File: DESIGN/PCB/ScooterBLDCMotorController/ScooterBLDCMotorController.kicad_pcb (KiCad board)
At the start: 2 copper layers, 210.3 x 103.4 mm, 30 parts, among them J1 M1 OUTPUT, J10 RC_ENABLE, J2 M1 INPUT, J3 M2 INPUT, J4 M2 OUTPUT, J5 I2C, J6 TEST SWITCH, J7 RC CH 1, J8 RC CH 2, J9 RC_PWR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

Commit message: Latest PCB and Rev1.0 release
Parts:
- added J11: TO M2 ENCODER, Connector_JST:JST_XH_B5B-XH-A_1x05_P2.50mm_Vertical, F.Cu at (186.4, 107.1)
- added J12: M2 INPUT, Connector_JST:JST_XH_B5B-XH-A_1x05_P2.50mm_Vertical, F.Cu at (162.1, 136.5)
- added REF**: MountingHole_4.5mm, MountingHole:MountingHole_4.5mm, F.Cu at (247.1, 140.2)
- added REF**: MountingHole_3.2mm_M3, MountingHole:MountingHole_3.2mm_M3, F.Cu at (246.9, 119.0)
- added REF**: MountingHole_3.2mm_M3, MountingHole:MountingHole_3.2mm_M3, F.Cu at (50.0, 62.5)
- added REF**: MountingHole_4.5mm, MountingHole:MountingHole_4.5mm, F.Cu at (247.9, 43.7)
- added REF**: MountingHole_3.2mm_M3, MountingHole:MountingHole_3.2mm_M3, F.Cu at (208.4, 62.7)
- added REF**: MountingHole_3.2mm_M3, MountingHole:MountingHole_3.2mm_M3, F.Cu at (88.4, 118.8)
- added REF**: MountingHole_3.2mm_M3, MountingHole:MountingHole_3.2mm_M3, F.Cu at (197.3, 124.6)
- added REF**: MountingHole_4.5mm, MountingHole:MountingHole_4.5mm, F.Cu at (50.8, 43.7)
- added REF**: MountingHole_3.2mm_M3, MountingHole:MountingHole_3.2mm_M3, F.Cu at (100.3, 68.6)
- added REF**: MountingHole_3.2mm_M3, MountingHole:MountingHole_3.2mm_M3, F.Cu at (197.3, 68.6)
- added REF**: MountingHole_4.5mm, MountingHole:MountingHole_4.5mm, F.Cu at (50.0, 140.2)
- added REF**: MountingHole_3.2mm_M3, MountingHole:MountingHole_3.2mm_M3, F.Cu at (100.3, 124.6)
- J2: value M1 INPUT -> TO M1 ENCODER; footprint Connector_JST:JST_XH_B3B-XH-A_1x03_P2.50mm_Vertical -> Connector_JST:JST_XH_B5B-XH-A_1x05_P2.50mm_Vertical
- J3: value M2 INPUT -> M1 INPUT; footprint Connector_JST:JST_XH_B3B-XH-A_1x03_P2.50mm_Vertical -> Connector_JST:JST_XH_B5B-XH-A_1x05_P2.50mm_Vertical
- R1: footprint Resistor_THT:R_Axial_DIN0204_L3.6mm_D1.6mm_P5.08mm_Vertical -> Resistor_THT:R_Axial_DIN0204_L3.6mm_D1.6mm_P7.62mm_Horizontal
- moved J2 46.1 mm to (112.0, 97.0), turned to -90 degrees
- moved J3 29.3 mm to (133.3, 136.3)
- moved J1 9.76 mm to (115.9, 136.3)
- moved C1 5.76 mm to (139.2, 129.7)
- moved C2 5.76 mm to (139.2, 133.7)
- moved C3 5.76 mm to (139.2, 137.8)
- moved J5 5.63 mm to (157.6, 47.8)
- moved J6 5.63 mm to (111.8, 68.4)
- moved J7 5.63 mm to (134.7, 52.9)
- moved U10 5.63 mm to (127.5, 66.7)
- moved U2 5.63 mm to (141.0, 116.7)
- moved U3 5.63 mm to (150.2, 107.8)
- moved U5 5.63 mm to (165.4, 116.7)
- moved U7 5.63 mm to (167.2, 78.6)
- moved U8 5.63 mm to (167.2, 88.3)
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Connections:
- J2 pad 1: /M1 Y -> Net-(J2-Pad1)
- J2 pad 2: /M1 B -> /M1 Y
- J2 pad 3: /M1 G -> /M1 B
- J3 pad 1: /M2 Y -> Net-(J2-Pad1)
- J3 pad 2: /M2 B -> /M1 Y
- J3 pad 3: /M2 G -> /M1 B
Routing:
- net Net-(J11-Pad5): track 0.00 -> 80.2 mm
- net /M2 G: track 31.5 -> 100.9 mm
- net /M2 B: track 27.3 -> 75.7 mm
- net Net-(J2-Pad1): track 0.00 -> 48.1 mm
- net /M1 Y: track 25.8 -> 70.7 mm
- net /M2 Y: track 24.6 -> 69.1 mm
- net Net-(J11-Pad1): track 0.00 -> 39.5 mm
- net /M1 B: track 29.6 -> 68.7 mm
- net /M1 G: track 30.3 -> 65.6 mm
- net Net-(J2-Pad5): track 0.00 -> 33.9 mm
- net Net-(J6-Pad1): track 53.9 -> 57.5 mm
- net /3v: track 168.1 -> 170.1 mm, vias 1 -> 0
- net /M2 SPEED: track 27.8 -> 29.7 mm
- net /M2 BRAKE: track 27.8 -> 29.7 mm
- net /M2 DIR: track 33.4 -> 35.3 mm
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- added copper zone on B.Cu, net /GND
- added copper zone on F.Cu, net /GND
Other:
- board size 210.3 x 103.4 mm -> 210.3 x 109 mm
- board text added: "BLDC MOTOR CONTROLLER REV 1.0"
- board text added: "M1 CONTROLLER"
- board text added: "M2 CONTROLLER"
- board text added: "TO M1 ENCODERS"
- board text added: "TO M2 ENCODERS"

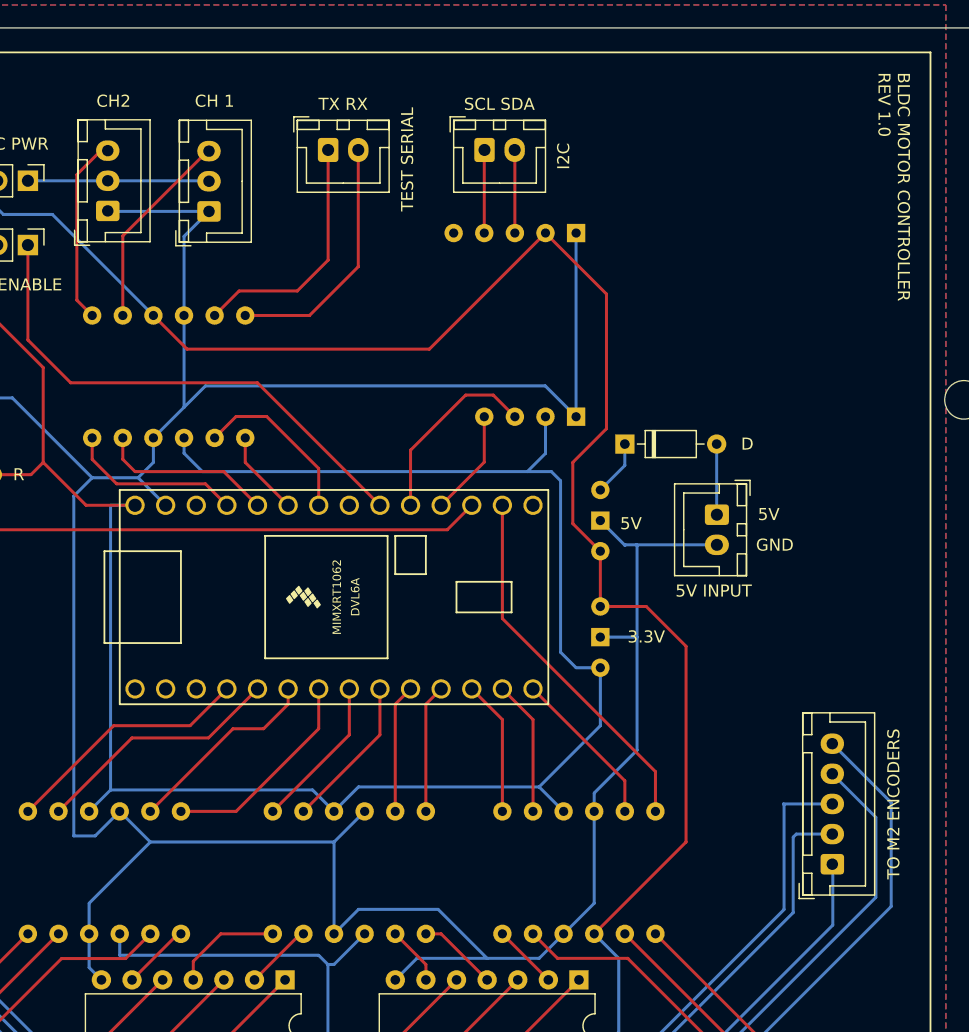
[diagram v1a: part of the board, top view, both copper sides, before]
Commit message: Fixed swapped connections on level shifter.
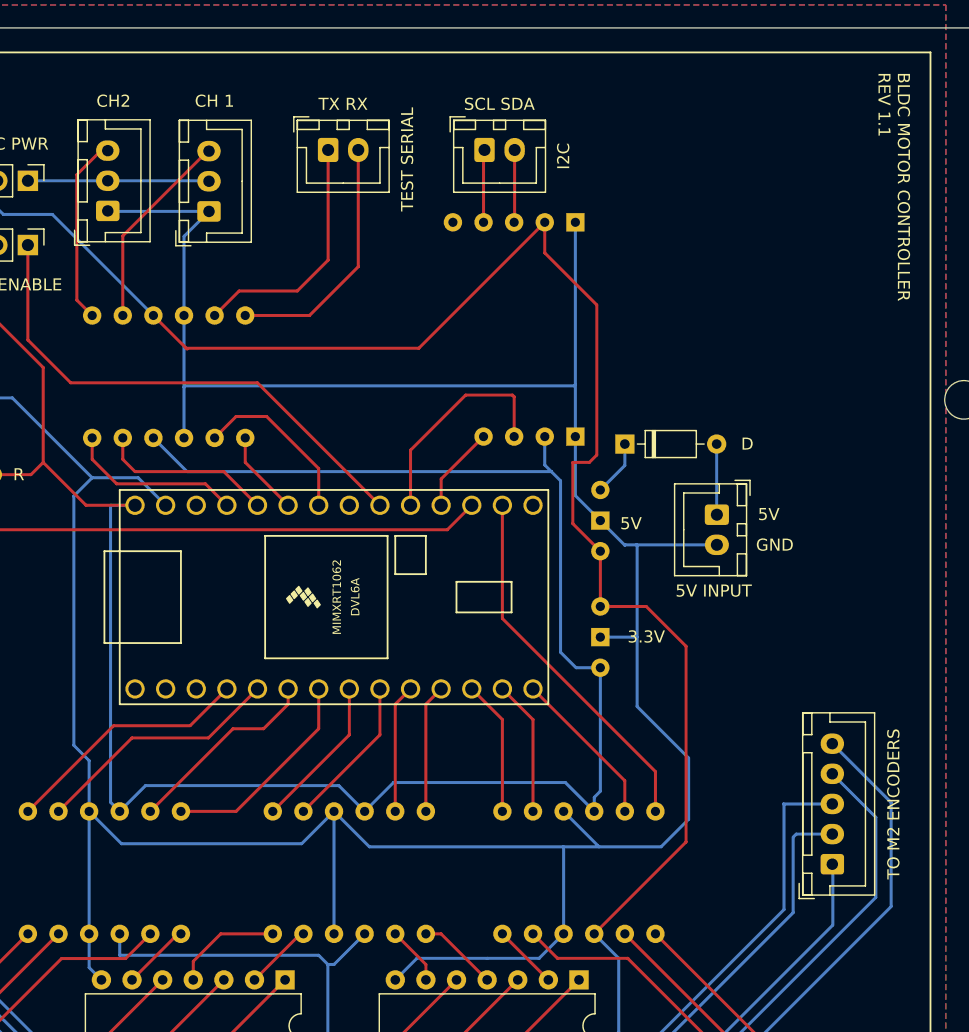
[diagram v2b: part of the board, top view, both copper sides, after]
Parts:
- moved U9 1.65 mm to (162.6, 64.0)
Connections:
- U1 pad 10: /3v -> /GND
- U1 pad 9: /GND -> /3v
- U10 pad 10: /3v -> /GND
- U10 pad 9: /GND -> /3v
- U3 pad 10: /3v -> /GND
- U3 pad 9: /GND -> /3v
- U6 pad 10: /3v -> /GND
- U6 pad 9: /GND -> /3v
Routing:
- net /GND: track 261.1 -> 279.3 mm
- net /3v: track 170.1 -> 172.7 mm
- net Net-(U4-Pad24): track 15.9 -> 18.4 mm
- net Net-(U4-Pad23): track 8.83 -> 7.15 mm
- net /5v: track 233.4 -> 234.8 mm
- net Net-(J5-Pad2): track 6.87 -> 6.02 mm
- net Net-(J5-Pad1): track 6.87 -> 6.04 mm
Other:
- board text added: "BLDC MOTOR CONTROLLER REV 1.1"
- board text removed: "BLDC MOTOR CONTROLLER REV 1.0"

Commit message: Revision 1.2 of MotorController board
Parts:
- added J13: Conn_01x01_Male, Connector_PinHeader_2.54mm:PinHeader_1x01_P2.54mm_Vertical, F.Cu at (111.5, 135.4)
- added J14: Conn_01x01_Male, Connector_PinHeader_2.54mm:PinHeader_1x01_P2.54mm_Vertical, F.Cu at (186.7, 82.8)
- U7: value 5V_Voltage_Regulator -> (none); footprint Custom:Voltage Regulator -> Custom:Level Shifter
- U8: value 3.3V_Voltage_Regulator -> 5V_StepUpDown_Voltage_Regulator; footprint Custom:Voltage Regulator -> Custom:StepUpDown Voltage Regulator
- U9: value (none) -> 3V_StepUpDown_Voltage_Regulator; footprint Custom:I2C Level Shifter -> Custom:StepUpDown Voltage Regulator
- moved J4 93.4 mm to (201.9, 44.5), turned to -90 degrees
- moved J1 89.3 mm to (95.8, 49.3), turned to 90 degrees
- moved U8 31.9 mm to (167.9, 56.4)
- moved D1 25.0 mm to (174.0, 47.8)
- moved POWER1 24.7 mm to (181.6, 53.8)
- moved U7 19.7 mm to (151.4, 66.8)
- moved U9 6.86 mm to (167.9, 68.3), turned to -90 degrees
- moved U4 5.29 mm to (150.4, 84.9)
- moved U1 4.53 mm to (130.8, 103.4)
- moved U3 4.53 mm to (151.1, 103.4)
- moved U6 4.53 mm to (170.2, 103.4)
- moved J6 0.21 mm to (112.0, 68.4)
- moved R1 0.21 mm to (117.0, 74.8)
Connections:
- U7 pad 1: Net-(D1-Pad1) -> unconnected-(U7-Pad1)
- U7 pad 2: /GND -> unconnected-(U7-Pad2)
- U7 pad 3: /5v -> /GND
- U8 pad 1: /5v -> Net-(D1-Pad1)
- U8 pad 3: /3v -> /5v
- U9 pad 2: Net-(U4-Pad23) -> /GND
- U9 pad 3: Net-(U4-Pad24) -> /3v
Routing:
- net /GND: track 279.3 -> 53.6 mm
- net /M1 SPEED: track 32.3 -> 93.3 mm
- net /M1 BRAKE: track 27.1 -> 87.5 mm
- net /M1 DIR: track 27.0 -> 85.7 mm
- net /M2 SPEED: track 29.7 -> 81.4 mm
- net /M2 DIR: track 35.3 -> 86.8 mm
- net /M2 BRAKE: track 29.7 -> 75.5 mm
- net /3v: track 172.7 -> 152.4 mm
- net /5v: track 234.8 -> 247.5 mm
- net Net-(J5-Pad2): track 6.02 -> 17.5 mm
- net Net-(J5-Pad1): track 6.04 -> 17.5 mm
- net Net-(U4-Pad24): track 18.4 -> 10.1 mm
- net Net-(U4-Pad21): track 30.7 -> 24.4 mm
- net Net-(U4-Pad14): track 13.3 -> 7.10 mm
- net Net-(J10-Pad1): track 42.8 -> 48.1 mm
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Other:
- board text added: "BLDC MOTOR CONTROLLER REV 1.2"
- board text removed: "BLDC MOTOR CONTROLLER REV 1.1"

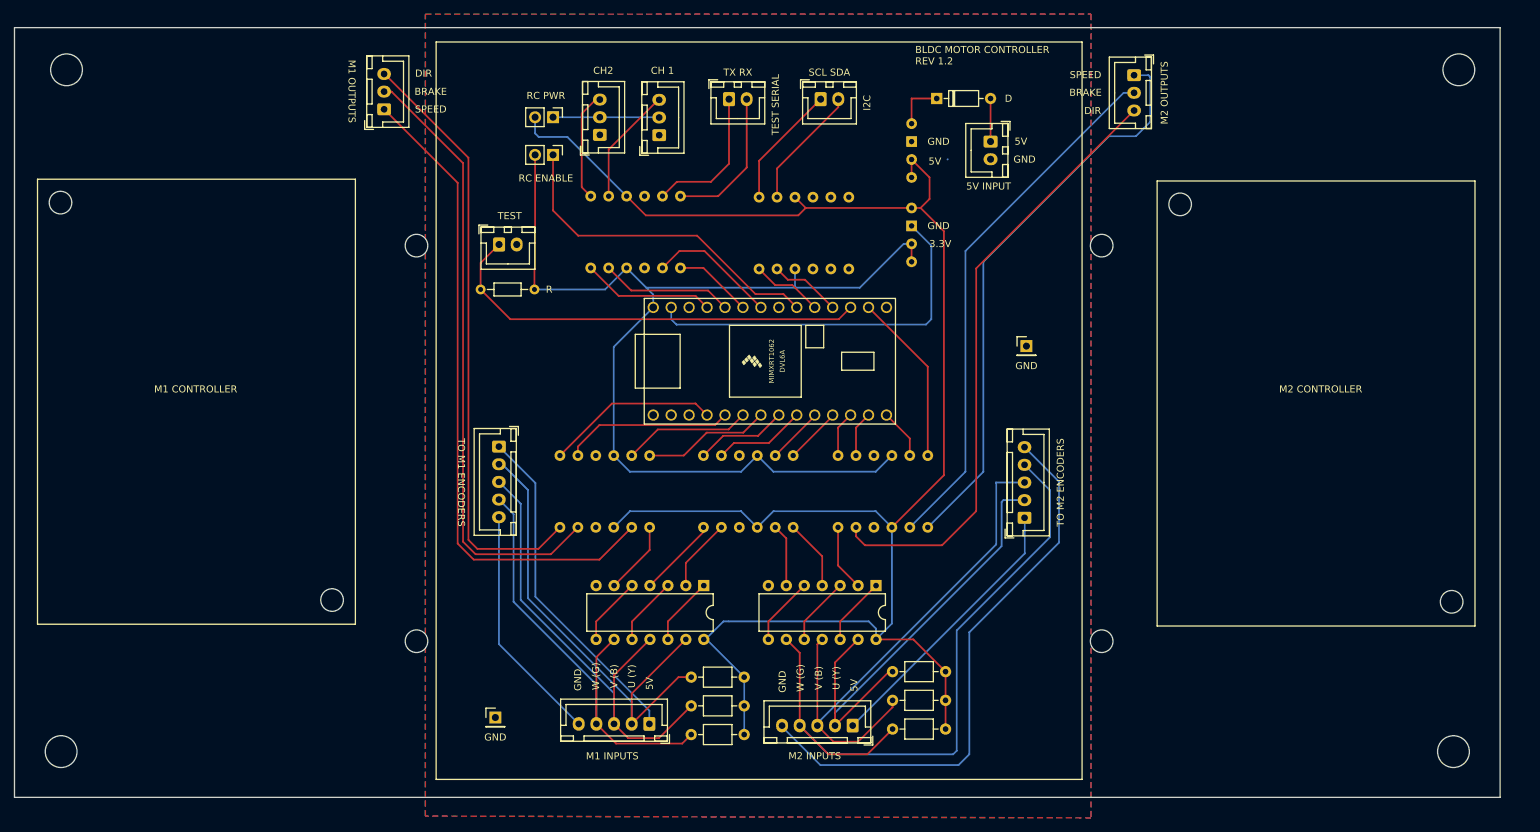
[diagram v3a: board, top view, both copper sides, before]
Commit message: Updated PCB to use terminals, added new DriveByRC code
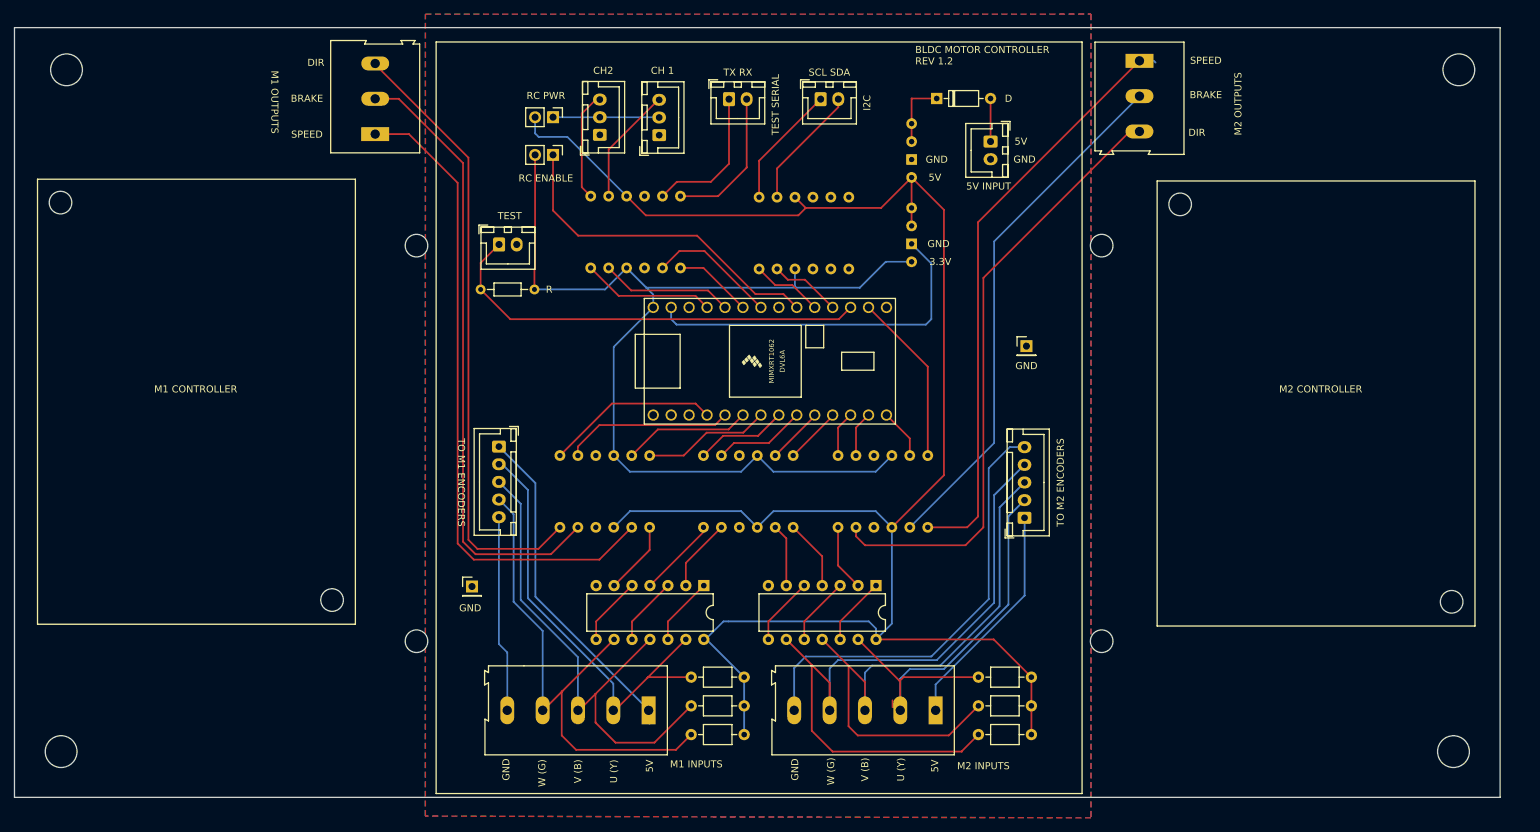
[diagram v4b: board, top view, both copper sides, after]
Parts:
- J1, J4: footprint Connector_JST:JST_XH_B3B-XH-A_1x03_P2.50mm_Vertical -> TerminalBlock:TerminalBlock_Altech_AK300-3_P5.00mm
- J12, J3: footprint Connector_JST:JST_XH_B5B-XH-A_1x05_P2.50mm_Vertical -> Custom:TerminalBlock_Altech_AK300-5_P5.00mm
- moved J13 18.8 mm to (108.2, 116.8)
- moved C4 12.2 mm to (179.9, 129.7)
- moved C5 12.2 mm to (187.4, 133.7)
- moved C6 12.2 mm to (187.4, 137.8)
- moved J12 11.9 mm to (173.8, 134.4)
- moved J1 3.74 mm to (94.5, 52.8)
- moved J4 2.17 mm to (202.7, 42.4)
- moved J3 1.92 mm to (133.2, 134.4)
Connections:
- U8 pad 2: /GND -> Net-(D1-Pad1)
- U8 pad 3: /5v -> /GND
- U9 pad 2: /GND -> /5v
- U9 pad 3: /3v -> /GND
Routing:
- net Net-(J11-Pad5): track 80.2 -> 62.4 mm
- net /5v: track 247.5 -> 261.2 mm
- net /M2 B: track 75.7 -> 89.0 mm
- net /M1 Y: track 70.7 -> 62.0 mm
- net /M1 G: track 65.6 -> 73.0 mm
- net Net-(J11-Pad1): track 39.5 -> 32.5 mm
- net Net-(J2-Pad5): track 33.9 -> 27.8 mm
- net /M2 Y: track 69.1 -> 64.7 mm
- net /3v: track 152.4 -> 148.8 mm
- net /M1 B: track 68.7 -> 72.3 mm
- net Net-(D1-Pad1): track 7.11 -> 9.65 mm
- net /GND: track 53.6 -> 51.0 mm
- net /M1 DIR: track 85.7 -> 87.7 mm
- net /M2 G: track 100.9 -> 102.1 mm
- net /M2 BRAKE: track 75.5 -> 74.5 mm
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
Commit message: Revision 1.3 for PCB
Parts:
- added J15: RC CH 3, Connector_JST:JST_XH_B3B-XH-A_1x03_P2.50mm_Vertical, F.Cu at (120.8, 52.9)
- added R2: R, Resistor_THT:R_Axial_DIN0204_L3.6mm_D1.6mm_P7.62mm_Horizontal, F.Cu at (159.0, 54.6)
- added R3: R, Resistor_THT:R_Axial_DIN0204_L3.6mm_D1.6mm_P7.62mm_Horizontal, F.Cu at (159.0, 57.8)
- moved J9 7.15 mm to (112.5, 50.3)
- moved J10 7.15 mm to (112.5, 55.7)
- moved J5 3.85 mm to (161.4, 47.8)
- moved SERIAL1 3.85 mm to (148.4, 47.8)
- moved J8 2.91 mm to (129.2, 52.9)
- moved J7 2.71 mm to (137.4, 52.9)
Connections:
- J5 pad 1: Net-(J5-Pad1) -> Net-(J5-Pin_1)
- J5 pad 2: Net-(J5-Pad2) -> Net-(J5-Pin_2)
- U4 pad 23: Net-(U4-Pad23) -> Net-(J5-Pin_1)
- U4 pad 24: Net-(U4-Pad24) -> Net-(J5-Pin_2)
- U4 pad 26: unconnected-(U4-Pad26) -> Net-(U4-19_A5_SCL0)
- U7 pad 5: Net-(J5-Pad2) -> unconnected-(U7-HV2-Pad5)
- U7 pad 6: Net-(J5-Pad1) -> Net-(J15-Pin_3)
- U7 pad 7: Net-(U4-Pad24) -> Net-(U4-19_A5_SCL0)
- U7 pad 8: Net-(U4-Pad23) -> unconnected-(U7-LV2-Pad8)
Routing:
- net Net-(J5-Pin_2): track 0.00 -> 49.7 mm, vias 0 -> 1
- net Net-(J15-Pin_3): track 0.00 -> 45.0 mm
- net Net-(J5-Pin_1): track 0.00 -> 37.1 mm, vias 0 -> 1
- net /3v: track 148.8 -> 169.2 mm
- net Net-(J5-Pad1): track 17.5 -> 0.00 mm
- net Net-(J5-Pad2): track 17.5 -> 0.00 mm
- net Net-(U4-Pad23): track 10.1 -> 0.00 mm
- net Net-(U4-Pad24): track 10.1 -> 0.00 mm
- net Net-(J15-Pin_2): track 15.0 -> 25.0 mm
- net /5v: track 261.2 -> 270.6 mm
- net Net-(U4-19_A5_SCL0): track 0.00 -> 6.60 mm
- net Net-(J10-Pin_1): track 48.1 -> 51.1 mm
- net /TX: track 20.5 -> 22.1 mm
- net /RX: track 20.8 -> 22.3 mm
- net Net-(J7-Pin_3): track 16.5 -> 17.8 mm
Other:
- board text added: "BLDC MOTOR CONTROLLER REV 1.3"
- board text added: "CH 2"
- board text added: "CH 3"
- board text added: "PULLUPS"
- board text removed: "BLDC MOTOR CONTROLLER REV 1.2"
- board text removed: "CH2"
